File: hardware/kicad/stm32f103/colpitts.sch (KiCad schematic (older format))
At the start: 42 parts, among them P2 LOOP1, P3 LOOP2, Q1 BSS138, Q2 BC817-40, Q3 BSS138, Q4 BC817-40, T1 78601/9C, T2 78601/9C

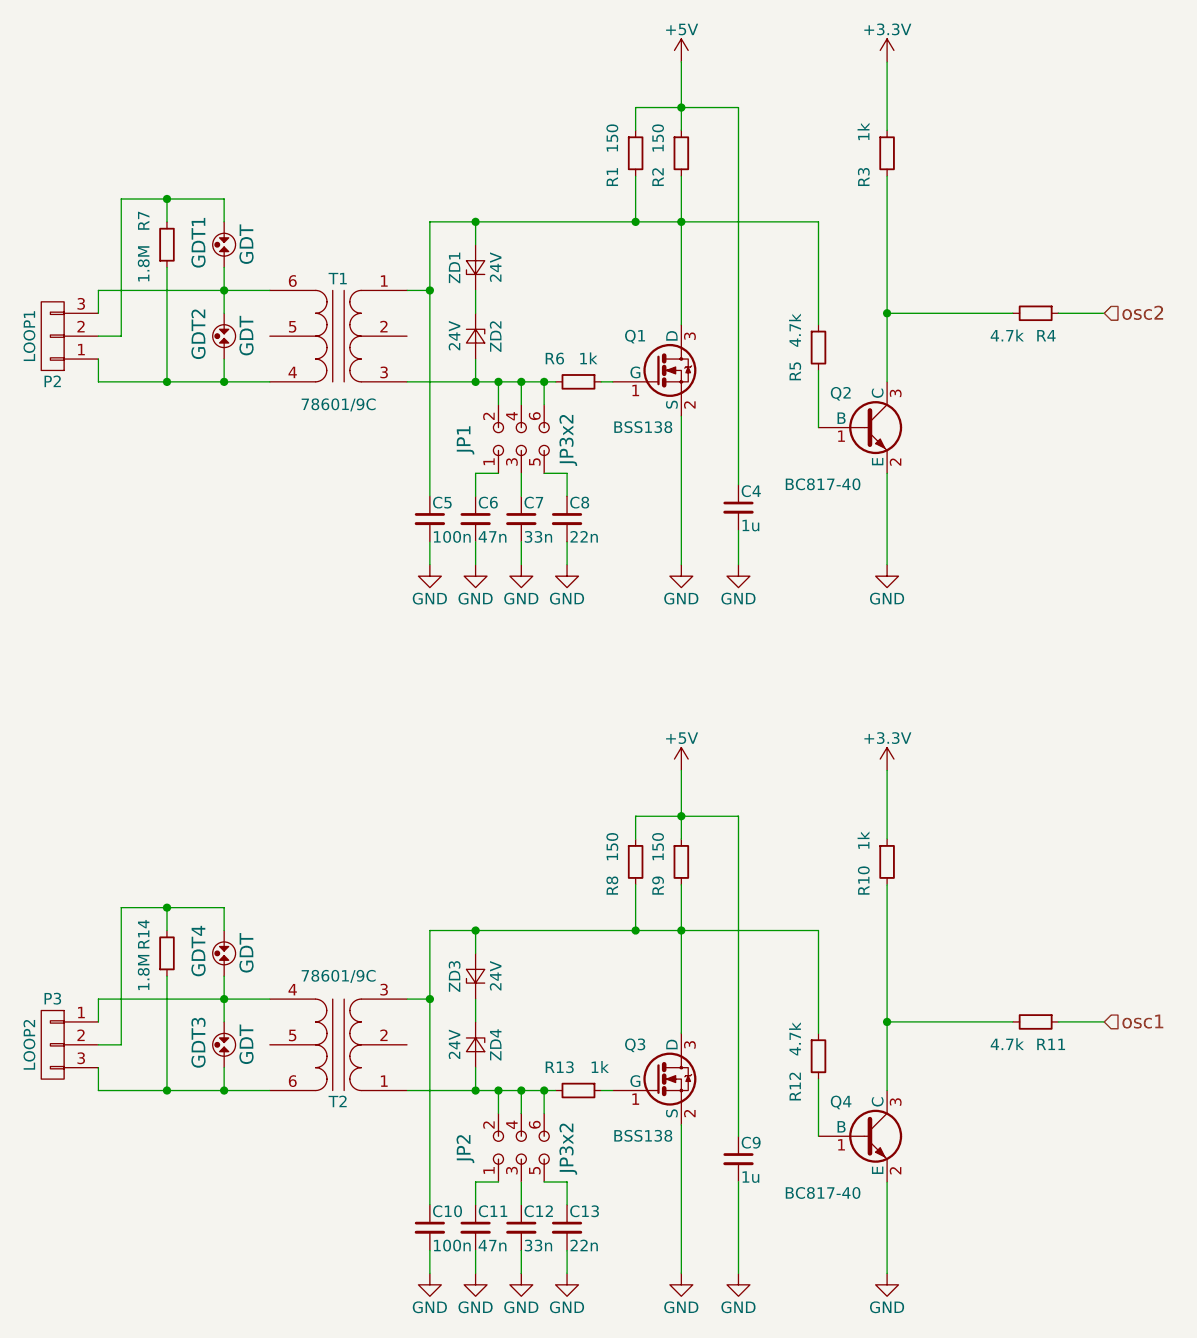
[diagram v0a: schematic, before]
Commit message: hardware/kicad/stm32f103: MCU/LED block ready
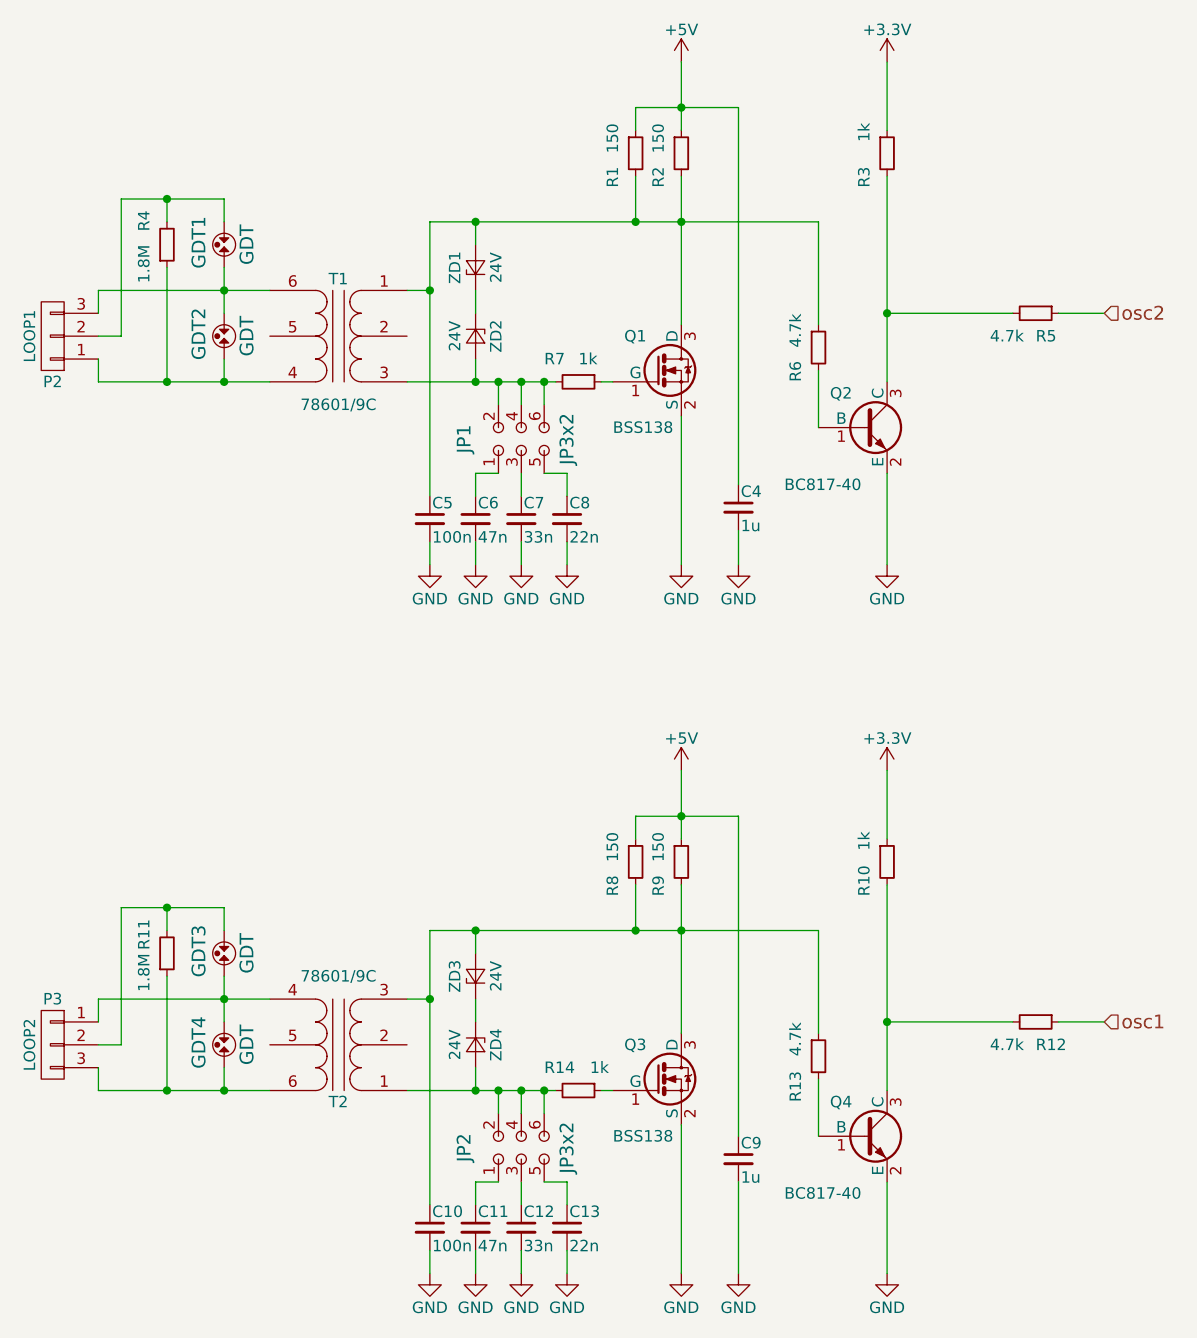
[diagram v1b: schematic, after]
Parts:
- renumbered GDT4 to GDT3, GDT3 to GDT4, R14 to R11, R11 to R12, R12 to R13, R13 to R14, R7 to R4, R4 to R5, R5 to R6, R6 to R7
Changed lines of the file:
@@
 LIBS:transformer
 LIBS:stm32
-LIBS:stm32f030-cache
+LIBS:stm32f103-cache
 EELAYER 25 0
 EELAYER END
 $Descr A4 11693 8268
 encoding utf-8
-Sheet 2 6
+Sheet 2 5
 Title ""
 Date ""
@@
 $EndComp
 $Comp
-L R_Small R14
+L R_Small R11
 U 1 1 588475BA
 P 1850 5250
-F 0 "R14" V 1750 5100 50  0000 L CNN
+F 0 "R11" V 1750 5100 50  0000 L CNN
 F 1 "1.8M" V 1750 5250 50  0000 L CNN
 F 2 "Resistors_SMD:R_0603_HandSoldering" H 1850 5250 50  0001 C CNN
@@
 $EndComp
 $Comp
-L GDT GDT3
+L GDT GDT4
 U 1 1 588475BC
 P 2100 5650
-F 0 "GDT3" H 2110 5540 60  0000 C CNN
+F 0 "GDT4" H 2110 5540 60  0000 C CNN
 F 1 "GDT" H 2100 5750 60  0000 C CNN
 F 2 "cardetector:GDT" H 2225 5825 60  0001 C CNN
@@
 $EndComp
 $Comp
-L GDT GDT4
+L GDT GDT3
 U 1 1 588475BD
 P 2100 5250
-F 0 "GDT4" H 2110 5140 60  0000 C CNN
+F 0 "GDT3" H 2110 5140 60  0000 C CNN
 F 1 "GDT" H 2100 5350 60  0000 C CNN
 F 2 "cardetector:GDT" H 2225 5425 60  0001 C CNN
@@
 $EndComp
 $Comp
-L R_Small R13
+L R_Small R14
 U 1 1 588475C9
 P 3650 5850
-F 0 "R13" V 3550 5700 50  0000 L CNN
+F 0 "R14" V 3550 5700 50  0000 L CNN
 F 1 "1k" V 3550 5900 50  0000 L CNN
 F 2 "Resistors_SMD:R_0603_HandSoldering" H 3650 5850 50  0001 C CNN
@@
 $EndComp
 $Comp
-L R_Small R12
+L R_Small R13
 U 1 1 588475CF
 P 4700 5700
-F 0 "R12" V 4600 5500 50  0000 L CNN
+F 0 "R13" V 4600 5500 50  0000 L CNN
 F 1 "4.7k" V 4600 5700 50  0000 L CNN
 F 2 "Resistors_SMD:R_0603_HandSoldering" H 4700 5700 50  0001 C CNN
@@
 $EndComp
 $Comp
-L R_Small R11
+L R_Small R12
 U 1 1 588475D8
 P 5650 5550
-F 0 "R11" V 5750 5550 50  0000 L CNN
+F 0 "R12" V 5750 5550 50  0000 L CNN
 F 1 "4.7k" V 5750 5350 50  0000 L CNN
 F 2 "Resistors_SMD:R_0603_HandSoldering" H 5650 5550 50  0001 C CNN
@@
 $EndComp
 $Comp
-L R_Small R7
+L R_Small R4
 U 1 1 5884A6D3
 P 1850 2150
-F 0 "R7" V 1750 2000 50  0000 L CNN
+F 0 "R4" V 1750 2000 50  0000 L CNN
 F 1 "1.8M" V 1750 2150 50  0000 L CNN
 F 2 "Resistors_SMD:R_0603_HandSoldering" H 1850 2150 50  0001 C CNN
@@
 $EndComp
 $Comp
-L R_Small R6
+L R_Small R7
 U 1 1 5884A729
 P 3650 2750
-F 0 "R6" V 3550 2600 50  0000 L CNN
+F 0 "R7" V 3550 2600 50  0000 L CNN
 F 1 "1k" V 3550 2750 50  0000 L CNN
 F 2 "Resistors_SMD:R_0603_HandSoldering" H 3650 2750 50  0001 C CNN
@@
 $EndComp
 $Comp
-L R_Small R5
+L R_Small R6
 U 1 1 5884A752
 P 4700 2600
-F 0 "R5" V 4600 2450 50  0000 L CNN
+F 0 "R6" V 4600 2450 50  0000 L CNN
 F 1 "4.7k" V 4600 2600 50  0000 L CNN
 F 2 "Resistors_SMD:R_0603_HandSoldering" H 4700 2600 50  0001 C CNN
@@
 $EndComp
 $Comp
-L R_Small R4
+L R_Small R5
 U 1 1 5884A779
 P 5650 2450
-F 0 "R4" V 5750 2450 50  0000 L CNN
+F 0 "R5" V 5750 2450 50  0000 L CNN
 F 1 "4.7k" V 5750 2250 50  0000 L CNN
 F 2 "Resistors_SMD:R_0603_HandSoldering" H 5650 2450 50  0001 C CNN
